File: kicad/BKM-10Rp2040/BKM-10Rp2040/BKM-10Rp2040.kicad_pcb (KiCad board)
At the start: 2 copper layers, 34.3 x 82.5 mm, 12 parts, among them J1 DB9_Female_MountingHoles, J2 Conn_01x04, SW1 SW_DPST_x2, U1 ADM3063EARZ-ND, U2 Pico, U3 TSOP335xx

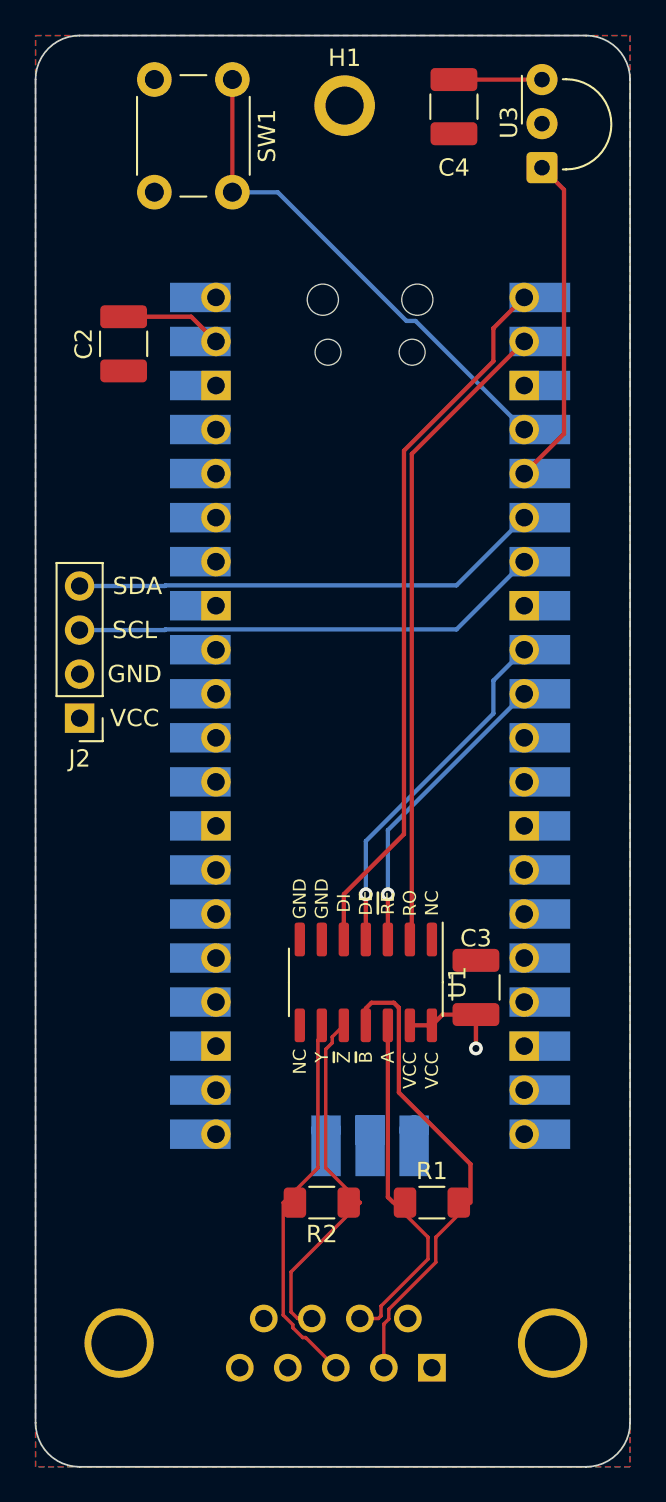
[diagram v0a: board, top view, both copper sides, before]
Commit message: fix rp2040 design
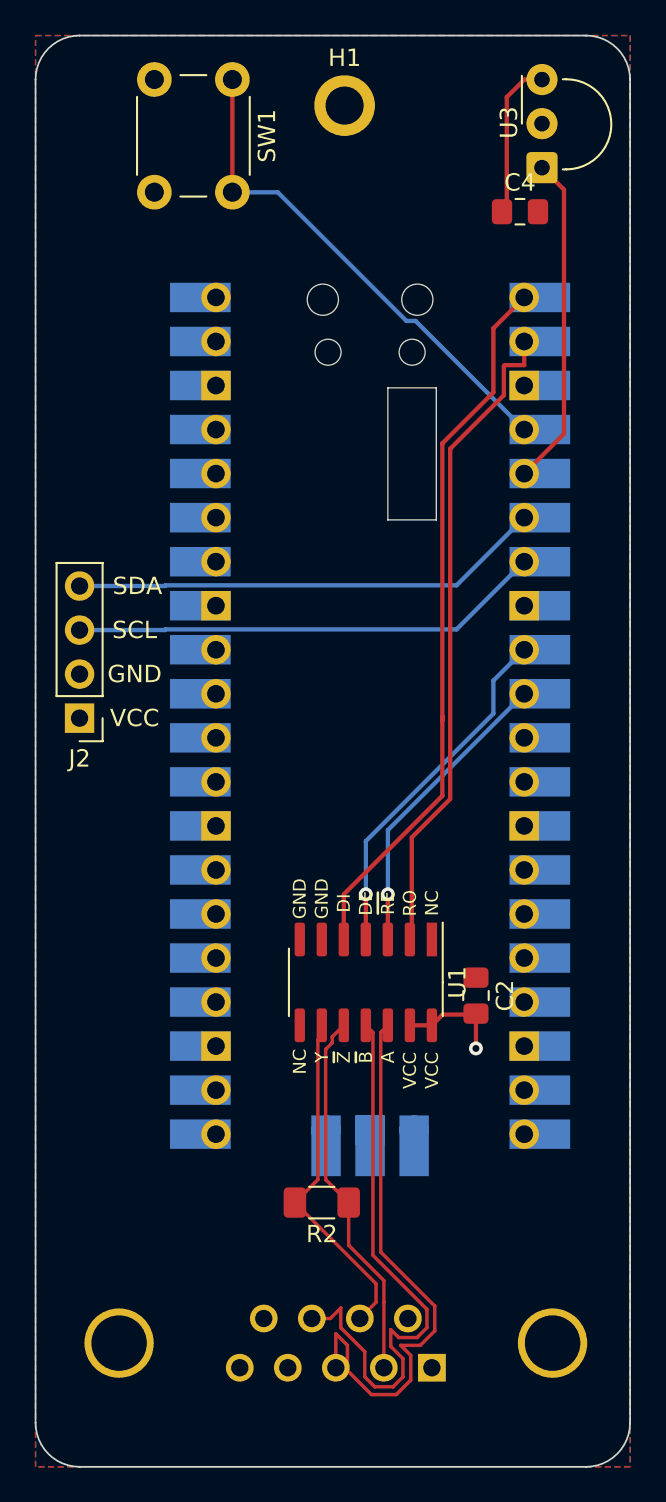
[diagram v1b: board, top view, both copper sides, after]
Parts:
- removed C3: 1uF, Capacitor_SMD:C_1210_3225Metric_Pad1.33x2.70mm_HandSolder
- removed R1: 60R, Resistor_SMD:R_1206_3216Metric_Pad1.30x1.75mm_HandSolder
- C2, C4: footprint Capacitor_SMD:C_1210_3225Metric_Pad1.33x2.70mm_HandSolder -> Capacitor_SMD:C_0805_2012Metric_Pad1.18x1.45mm_HandSolder
- moved C2 42.7 mm to (135.9, 116.3), turned to 270 degrees
- moved C4 7.16 mm to (138.4, 71.1), turned to 0 degrees
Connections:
- J1 pad 4: Net-(J1-Pad4) -> (no net)
- J1 pad 6: Net-(J1-Pad6) -> (no net)
- J1 pad 9: Net-(J1-Pad9) -> (no net)
- R2 pad 1: RXD- -> TXD-
- R2 pad 2: RXD+ -> TXD+
- U1 pad 1: Net-(U1-Pad1) -> (no net)
- U1 pad 10: RXD- -> TXD-
- U1 pad 11: TXD- -> RXD-
- U1 pad 12: TXD+ -> RXD+
- U1 pad 8: Net-(U1-Pad8) -> (no net)
- U1 pad 9: RXD+ -> TXD+
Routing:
- net RXD-: track 20.8 -> 33.6 mm
- net RXD+: track 22.0 -> 32.6 mm
- net TXD-: track 27.7 -> 21.6 mm
- net +5V: track 17.0 -> 15.2 mm
- net RX: track 37.0 -> 37.7 mm
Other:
- outline, holes or cut-outs redrawn
